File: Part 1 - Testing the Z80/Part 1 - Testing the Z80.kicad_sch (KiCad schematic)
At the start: 40 parts, among them J1 +5V DC, SW1 POWER, SW2 RESET, SW3 POWER, SW4 STEP, U1 Z80 CPU, U2 74LS175, U3 LMC555, U4 74HC14, U5 74HC74

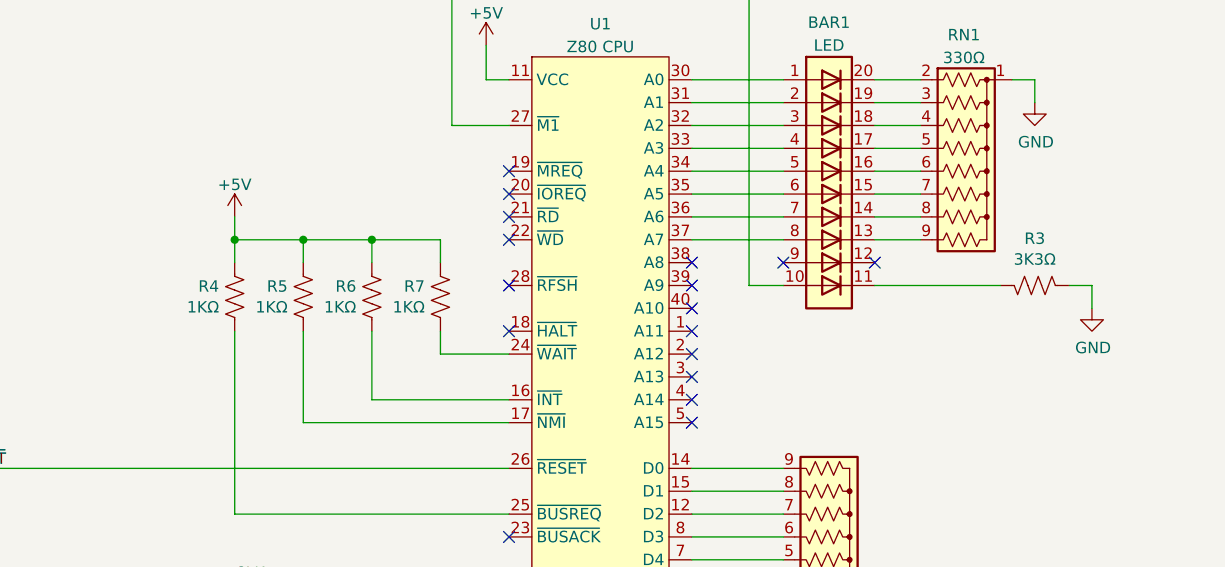
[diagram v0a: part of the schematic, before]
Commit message: Updating resistor values and added PDF schematic
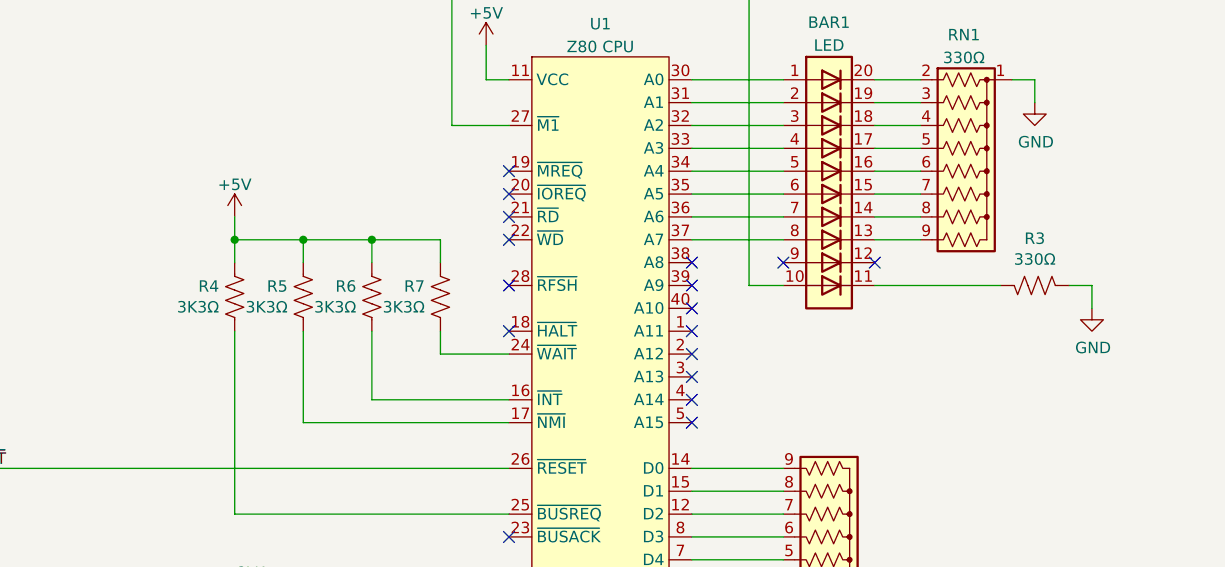
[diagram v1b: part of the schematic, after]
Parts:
- R3: value 3K3Ω -> 330Ω
- R4, R5, R6, R7: value 1KΩ -> 3K3Ω
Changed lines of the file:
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@@
       (effects (font (size 1.27 1.27)) (justify right))
     )
-    (property "Value" "1KΩ" (id 1) (at 132.8928 63.373 0)
+    (property "Value" "3K3Ω" (id 1) (at 132.8928 63.373 0)
       (effects (font (size 1.27 1.27)) (justify right))
     )
@@
       (effects (font (size 1.27 1.27)) (justify right))
     )
-    (property "Value" "1KΩ" (id 1) (at 148.1328 63.373 0)
+    (property "Value" "3K3Ω" (id 1) (at 148.1328 63.373 0)
       (effects (font (size 1.27 1.27)) (justify right))
     )
@@
     (in_bom yes) (on_board yes)
     (property "Reference" "R3" (id 0) (at 223.52 55.753 90))
-    (property "Value" "3K3Ω" (id 1) (at 223.52 58.0644 90))
+    (property "Value" "330Ω" (id 1) (at 223.52 58.0644 90))
     (property "Footprint" "Resistor_THT:R_Axial_DIN0207_L6.3mm_D2.5mm_P7.62mm_Horizontal" (id 2) (at 223.774 61.976 90)
       (effects (font (size 1.27 1.27)) hide)
@@
       (effects (font (size 1.27 1.27)) (justify right))
     )
-    (property "Value" "1KΩ" (id 1) (at 155.7528 63.373 0)
+    (property "Value" "3K3Ω" (id 1) (at 155.7528 63.373 0)
       (effects (font (size 1.27 1.27)) (justify right))
     )
@@
       (effects (font (size 1.27 1.27)) (justify right))
     )
-    (property "Value" "1KΩ" (id 1) (at 140.5128 63.373 0)
+    (property "Value" "3K3Ω" (id 1) (at 140.5128 63.373 0)
       (effects (font (size 1.27 1.27)) (justify right))
     )
@@
     )
     (path "/971cd676-8d4e-4185-98d3-78681d880ba1"
-      (reference "R3") (unit 1) (value "3K3Ω") (footprint "Resistor_THT:R_Axial_DIN0207_L6.3mm_D2.5mm_P7.62mm_Horizontal")
+      (reference "R3") (unit 1) (value "330Ω") (footprint "Resistor_THT:R_Axial_DIN0207_L6.3mm_D2.5mm_P7.62mm_Horizontal")
     )
     (path "/13a87942-83c3-4404-affc-55d1dcd6e7d0"
-      (reference "R4") (unit 1) (value "1KΩ") (footprint "Resistor_THT:R_Axial_DIN0207_L6.3mm_D2.5mm_P7.62mm_Horizontal")
+      (reference "R4") (unit 1) (value "3K3Ω") (footprint "Resistor_THT:R_Axial_DIN0207_L6.3mm_D2.5mm_P7.62mm_Horizontal")
     )
     (path "/c2bc0953-1542-4c2b-aba7-d01693a2c090"
-      (reference "R5") (unit 1) (value "1KΩ") (footprint "Resistor_THT:R_Axial_DIN0207_L6.3mm_D2.5mm_P7.62mm_Horizontal")
+      (reference "R5") (unit 1) (value "3K3Ω") (footprint "Resistor_THT:R_Axial_DIN0207_L6.3mm_D2.5mm_P7.62mm_Horizontal")
     )
     (path "/20c08cb0-2cb3-4512-bfa8-33b4e6c26875"
-      (reference "R6") (unit 1) (value "1KΩ") (footprint "Resistor_THT:R_Axial_DIN0207_L6.3mm_D2.5mm_P7.62mm_Horizontal")
+      (reference "R6") (unit 1) (value "3K3Ω") (footprint "Resistor_THT:R_Axial_DIN0207_L6.3mm_D2.5mm_P7.62mm_Horizontal")
     )
     (path "/a4059ee2-2f3d-4cec-a199-cb8095fc305a"
-      (reference "R7") (unit 1) (value "1KΩ") (footprint "Resistor_THT:R_Axial_DIN0207_L6.3mm_D2.5mm_P7.62mm_Horizontal")
+      (reference "R7") (unit 1) (value "3K3Ω") (footprint "Resistor_THT:R_Axial_DIN0207_L6.3mm_D2.5mm_P7.62mm_Horizontal")
     )
     (path "/ebb5b167-ff6b-4790-a7d2-860d9d558923"

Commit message: Finished clock in part 2, added part 3
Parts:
- removed R3: 330Ω, Resistor_THT:R_Axial_DIN0207_L6.3mm_D2.5mm_P7.62mm_Horizontal, symbol Device:R_US
- RN1: value 330Ω -> 3K3Ω
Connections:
- net at BAR1.10 (A): no longer U1.27 (~{M1})
- no-connect marks 25 -> 28
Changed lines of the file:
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@@
   (no_connect (at 100.33 73.66))
   (no_connect (at 165.1 88.9))
+  (no_connect (at 205.74 60.96))
+  (no_connect (at 195.58 60.96))
+  (no_connect (at 165.1 43.18))
   (no_connect (at 198.12 129.54))
   (no_connect (at 198.12 134.62))
@@
     (stroke (width 0) (type default) (color 0 0 0 0))
   )
-  (wire (pts (xy 158.75 26.67) (xy 191.77 26.67))
-    (stroke (width 0) (type default) (color 0 0 0 0))
-  )
   (wire (pts (xy 71.12 91.44) (xy 71.12 118.11))
     (stroke (width 0) (type default) (color 0 0 0 0))
@@
     (stroke (width 0) (type default) (color 0 0 0 0))
   )
-  (wire (pts (xy 229.87 60.96) (xy 229.87 63.5))
-    (stroke (width 0) (type default) (color 0 0 0 0))
-  )
   (wire (pts (xy 205.74 50.8) (xy 210.82 50.8))
     (stroke (width 0) (type default) (color 0 0 0 0))
@@
     (stroke (width 0) (type default) (color 0 0 0 0))
   )
-  (wire (pts (xy 191.77 60.96) (xy 195.58 60.96))
-    (stroke (width 0) (type default) (color 0 0 0 0))
-  )
   (wire (pts (xy 71.12 54.61) (xy 71.12 81.28))
     (stroke (width 0) (type default) (color 0 0 0 0))
@@
     (stroke (width 0) (type default) (color 0 0 0 0))
   )
-  (wire (pts (xy 165.1 43.18) (xy 158.75 43.18))
-    (stroke (width 0) (type default) (color 0 0 0 0))
-  )
   (wire (pts (xy 165.1 38.1) (xy 162.56 38.1))
     (stroke (width 0) (type default) (color 0 0 0 0))
@@
     (stroke (width 0) (type default) (color 0 0 0 0))
   )
-  (wire (pts (xy 158.75 43.18) (xy 158.75 26.67))
-    (stroke (width 0) (type default) (color 0 0 0 0))
-  )
   (wire (pts (xy 40.64 88.9) (xy 60.96 88.9))
     (stroke (width 0) (type default) (color 0 0 0 0))
@@
     (stroke (width 0) (type default) (color 0 0 0 0))
   )
-  (wire (pts (xy 227.33 60.96) (xy 229.87 60.96))
-    (stroke (width 0) (type default) (color 0 0 0 0))
-  )
   (wire (pts (xy 74.93 138.43) (xy 92.71 138.43))
     (stroke (width 0) (type default) (color 0 0 0 0))
@@
     (stroke (width 0) (type default) (color 0 0 0 0))
   )
-  (wire (pts (xy 191.77 26.67) (xy 191.77 60.96))
-    (stroke (width 0) (type default) (color 0 0 0 0))
-  )
   (wire (pts (xy 40.64 91.44) (xy 40.64 88.9))
     (stroke (width 0) (type default) (color 0 0 0 0))
@@
   )
   (wire (pts (xy 134.62 55.88) (xy 134.62 58.42))
-    (stroke (width 0) (type default) (color 0 0 0 0))
-  )
-  (wire (pts (xy 205.74 60.96) (xy 219.71 60.96))
     (stroke (width 0) (type default) (color 0 0 0 0))
   )
@@
     (pin "1")
     (pin "2")
-  )
-  (symbol (lib_id "power:GND") (at 229.87 63.5 0) (unit 1)
-    (in_bom yes) (on_board yes)
-    (property "Reference" "#PWR09" (id 0) (at 229.87 69.85 0)
-      (effects (font (size 1.27 1.27)) hide)
-    )
-    (property "Value" "GND" (id 1) (at 229.997 67.8942 0))
-    (property "Footprint" "" (id 2) (at 229.87 63.5 0)
-      (effects (font (size 1.27 1.27)) hide)
-    )
-    (property "Datasheet" "" (id 3) (at 229.87 63.5 0)
-      (effects (font (size 1.27 1.27)) hide)
-    )
-    (pin "1")
   )
   (symbol (lib_id "Device:R_Network08_US") (at 200.66 88.9 270) (mirror x) (unit 1)
@@
     (in_bom yes) (on_board yes) (fields_autoplaced)
     (property "Reference" "RN1" (id 0) (at 215.646 33.1302 90))
-    (property "Value" "330Ω" (id 1) (at 215.646 35.6671 90))
+    (property "Value" "3K3Ω" (id 1) (at 215.646 35.6671 90))
     (property "Footprint" "Resistor_THT:R_Array_SIP9" (id 2) (at 215.9 60.325 90)
       (effects (font (size 1.27 1.27)) hide)
@@
     )
     (property "Datasheet" "~" (id 3) (at 134.62 153.67 0)
-      (effects (font (size 1.27 1.27)) hide)
-    )
-    (pin "1")
-    (pin "2")
-  )
-  (symbol (lib_id "Device:R_US") (at 223.52 60.96 90) (mirror x) (unit 1)
-    (in_bom yes) (on_board yes)
-    (property "Reference" "R3" (id 0) (at 223.52 55.753 90))
-    (property "Value" "330Ω" (id 1) (at 223.52 58.0644 90))
-    (property "Footprint" "Resistor_THT:R_Axial_DIN0207_L6.3mm_D2.5mm_P7.62mm_Horizontal" (id 2) (at 223.774 61.976 90)
-      (effects (font (size 1.27 1.27)) hide)
-    )
-    (property "Datasheet" "~" (id 3) (at 223.52 60.96 0)
       (effects (font (size 1.27 1.27)) hide)
     )
@@
       (reference "#PWR08") (unit 1) (value "+5V") (footprint "")
     )
-    (path "/0283445b-7fd6-4fcb-b5ed-cfc3a35fb4e7"
-      (reference "#PWR09") (unit 1) (value "GND") (footprint "")
-    )
     (path "/00000000-0000-0000-0000-000063c1f6ad"
       (reference "#PWR010") (unit 1) (value "GND") (footprint "")
@@
       (reference "R2") (unit 1) (value "10KΩ") (footprint "Resistor_THT:R_Axial_DIN0207_L6.3mm_D2.5mm_P10.16mm_Horizontal")
     )
-    (path "/971cd676-8d4e-4185-98d3-78681d880ba1"
-      (reference "R3") (unit 1) (value "330Ω") (footprint "Resistor_THT:R_Axial_DIN0207_L6.3mm_D2.5mm_P7.62mm_Horizontal")
-    )
     (path "/13a87942-83c3-4404-affc-55d1dcd6e7d0"
       (reference "R4") (unit 1) (value "3K3Ω") (footprint "Resistor_THT:R_Axial_DIN0207_L6.3mm_D2.5mm_P7.62mm_Horizontal")
@@
     )
     (path "/78a0fa50-e201-4f36-8240-703a3f865181"
-      (reference "RN1") (unit 1) (value "330Ω") (footprint "Resistor_THT:R_Array_SIP9")
+      (reference "RN1") (unit 1) (value "3K3Ω") (footprint "Resistor_THT:R_Array_SIP9")
     )
     (path "/1133043d-0035-4d61-801a-5bb9aa065492"
